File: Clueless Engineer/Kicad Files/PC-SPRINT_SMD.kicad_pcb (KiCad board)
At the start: 2 copper layers, 25 x 67 mm, 16 parts, among them J1 TB1, U1 8284A, U2 8284A, U3 8284A, X1 22.11 MHz

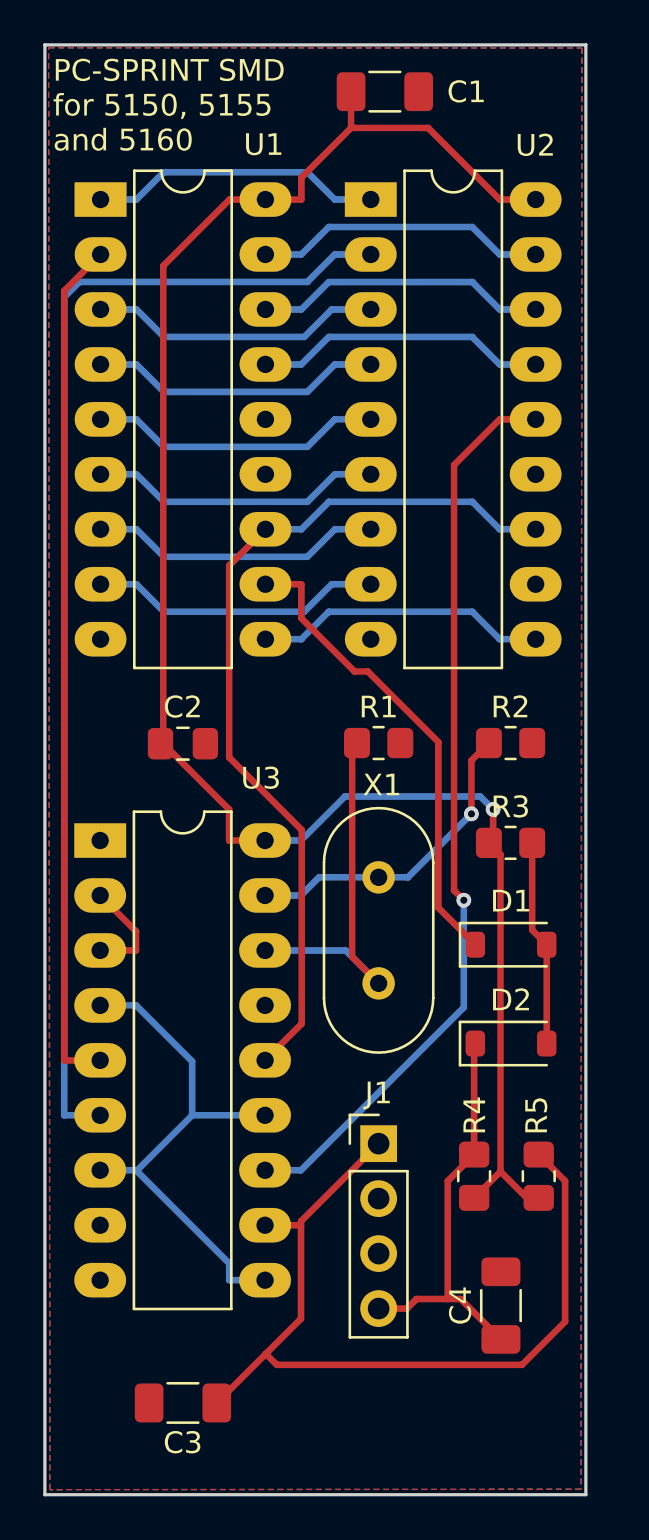
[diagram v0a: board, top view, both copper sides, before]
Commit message: Shrunk PCB to 24mm (from original 29.1mm)
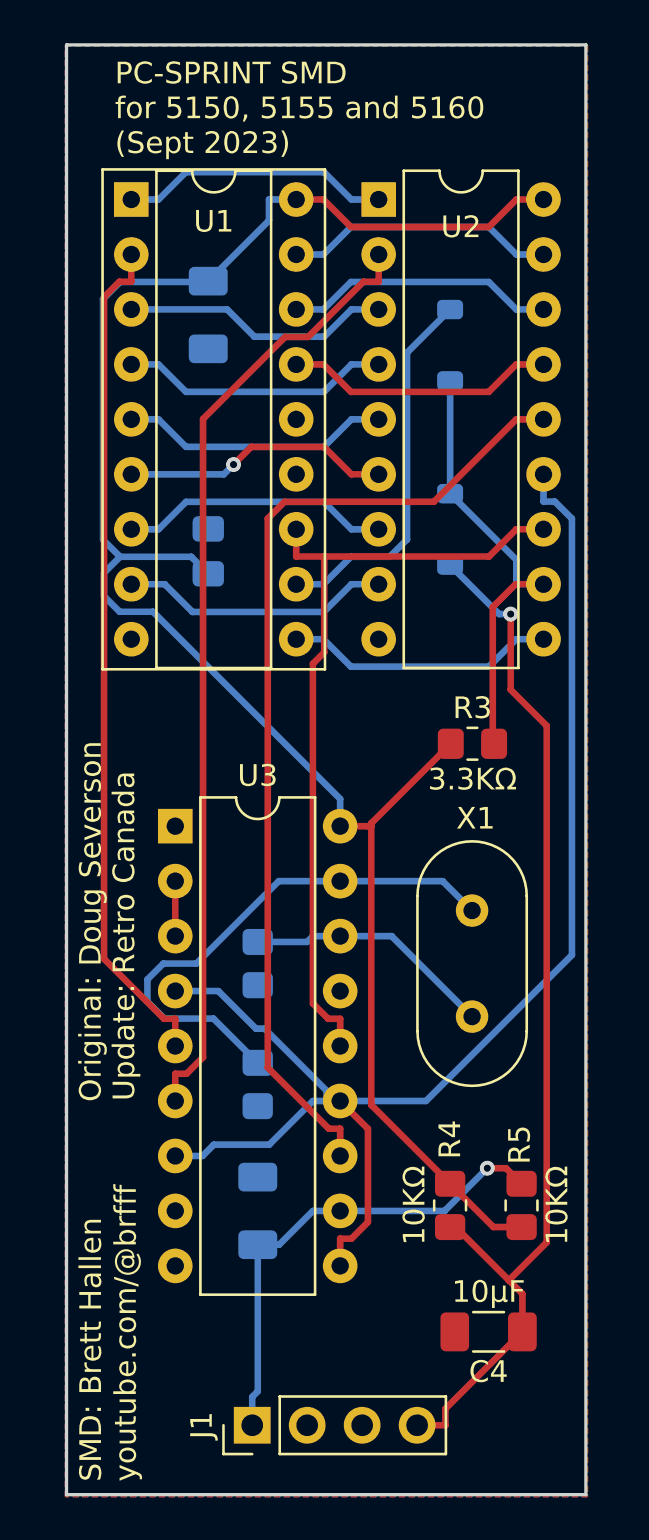
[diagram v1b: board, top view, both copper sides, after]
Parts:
- C1, C3: value 10uF -> 10µF; moved to B.Cu
- C2: value 0.01uF -> 100nF; moved to B.Cu
- C4: value 10uF -> 10µF
- D1, D2: moved to B.Cu
- R1, R2: value 560 -> 560Ω; moved to B.Cu
- R3: value 3.3K -> 3.3KΩ
- R4, R5: value 10K -> 10KΩ
- U1: footprint Package_DIP:DIP-18_W7.62mm_LongPads -> Package_DIP:DIP-18_W7.62mm_Socket
- U2, U3: footprint Package_DIP:DIP-18_W7.62mm_LongPads -> Package_DIP:DIP-18_W7.62mm
- moved D1 27.8 mm to (93.7, 63.9), turned to -90 degrees
- moved D2 23.9 mm to (93.7, 72.4), turned to 90 degrees
- moved R2 19.6 mm to (84.8, 98.0), turned to -90 degrees
- moved J1 14.3 mm to (84.6, 113.8), turned to 90 degrees
- moved C1 13.2 mm to (82.5, 62.5), turned to -90 degrees
- moved R1 11.6 mm to (84.8, 92.5), turned to -90 degrees
- moved C3 9.52 mm to (84.8, 103.9), turned to 90 degrees
- moved C2 8.96 mm to (82.5, 73.4), turned to 90 degrees
- moved R3 4.91 mm to (94.8, 82.3)
- moved X1 4.58 mm to (94.7, 94.9)
- moved U3 3.53 mm to (81.0, 86.1)
- moved R4 1.75 mm to (93.7, 103.6), turned to -90 degrees
- moved R5 1.57 mm to (97.0, 103.6)
- moved U1 1.42 mm to (79.0, 57.1)
- moved C4 1.34 mm to (95.5, 109.5), turned to 180 degrees
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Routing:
- net Net-(U2-F/C): track 25.0 -> 63.6 mm
- net Net-(D2-K): track 18.9 -> 49.4 mm, vias 0 -> 1
- net Net-(J1-Pin_1): track 39.8 -> 22.4 mm, vias 0 -> 1
- net Net-(D1-A): track 9.55 -> 21.0 mm
- net Net-(U2-PCLCK): track 54.4 -> 44.4 mm
- net Net-(U3-X1): track 14.7 -> 24.7 mm, vias 1 -> 0
- net Net-(U3-X2): track 17.6 -> 11.6 mm
- net Net-(D1-K): track 22.0 -> 17.4 mm
- net Net-(U1-OSC): track 40.9 -> 36.9 mm
- net Net-(U2-EFI): track 42.2 -> 45.8 mm, vias 1 -> 0
- net Net-(U3-PCLCK): track 4.89 -> 2.54 mm
- net Net-(U1-VCC): track 85.8 -> 87.6 mm, vias 1 -> 0
- net Net-(U1-~{AEN1}): track 13.5 -> 12.5 mm
- net Net-(U1-RESET): track 13.5 -> 12.5 mm
- net Net-(U1-~{ASYNC}): track 13.5 -> 12.5 mm
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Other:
- board size 25 x 67 mm -> 24 x 67 mm
- board text added: "PC-SPRINT SMD for 5150, 5155 and 5160 (Sept 2023)"
- board text removed: "PC-SPRINT SMD for 5150, 5155 and 5160"
